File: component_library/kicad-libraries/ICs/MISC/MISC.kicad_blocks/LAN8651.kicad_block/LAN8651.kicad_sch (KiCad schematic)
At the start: 7 parts, among them U1 LAN8651B1-E/LMX

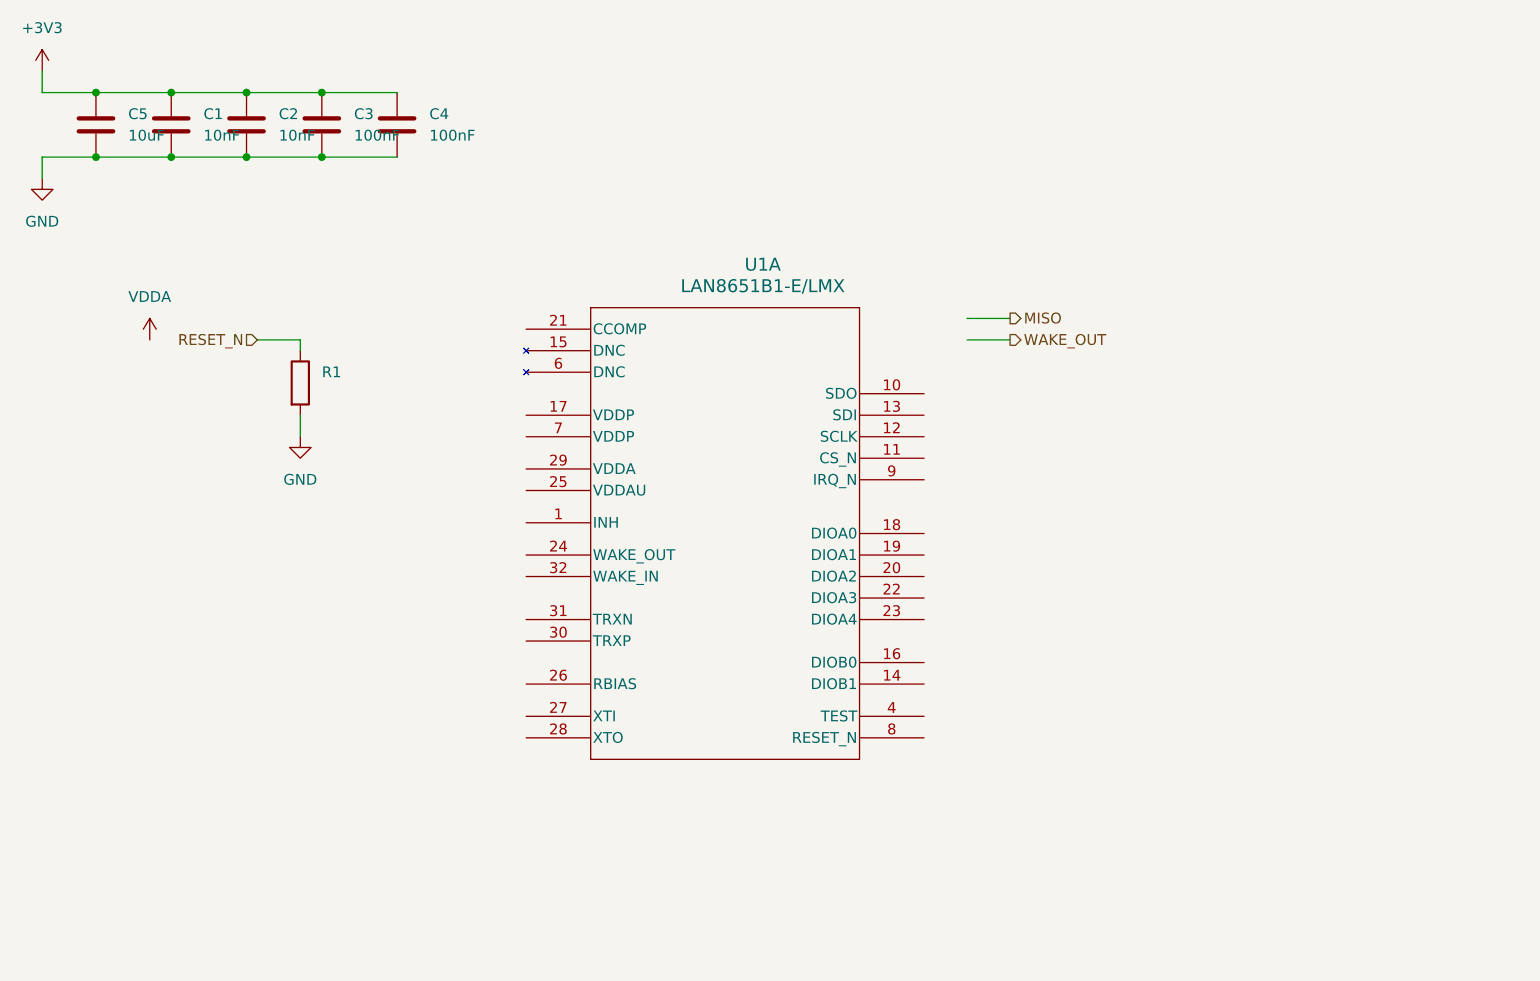
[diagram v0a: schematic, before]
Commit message: added crystal oscillator, finished schematic and layout
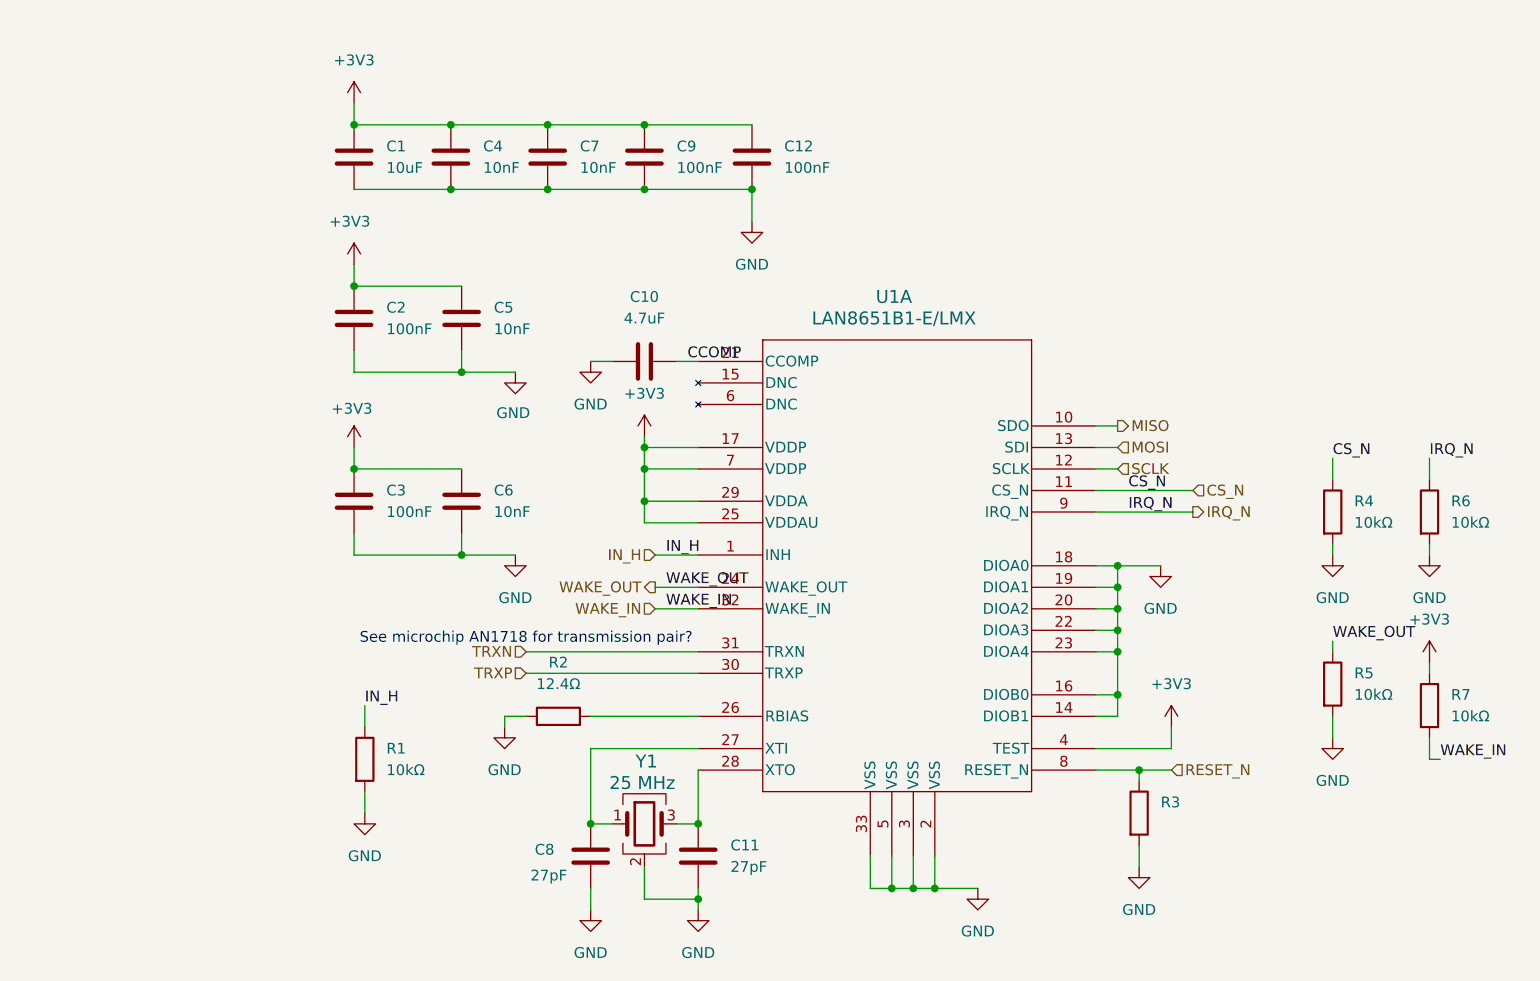
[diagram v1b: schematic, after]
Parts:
- removed C1, C2: 10nF, Capacitor_SMD:C_0402_1005Metric, symbol SSI_Passives:C 10nF 0402 50V X7R 10% Samsung
- removed C4: 100nF, Capacitor_SMD:C_0402_1005Metric, symbol SSI_Passives:C 100nF 0402 50V X7R 10% Samsung
- removed C5: 10uF, Capacitor_SMD:C_1210_3225Metric, symbol SSI_Passives:C 10uF 1210 25V X5R 10% Samsung
- added C1: 10uF, Capacitor_SMD:C_1210_3225Metric, symbol SSI_Passives:C 10uF 1210 25V X5R 10% Samsung
- added C10: 4.7uF, Capacitor_SMD:C_0402_1005Metric, symbol SSI_Passives:C 4.7uF 0402 10V X5R 20% Samsung
- added C11, C8: 27pF, Capacitor_SMD:C_0402_1005Metric, symbol SSI_Passives:C 27pF 0402 50V C0G 5% Samsung
- added C12, C2, C9: 100nF, Capacitor_SMD:C_0402_1005Metric, symbol SSI_Passives:C 100nF 0402 50V X7R 10% Samsung
- added C4, C5, C6, C7: 10nF, Capacitor_SMD:C_0402_1005Metric, symbol SSI_Passives:C 10nF 0402 50V X7R 10% Samsung
- added R2: 12.4Ω, Resistor_SMD:R_0402_1005Metric, symbol SSI_Passives:R 12.4 0402 1% Uniroyal
- added R3, R4, R5, R6, R7: 10kΩ, Resistor_SMD:R_0402_1005Metric, symbol SSI_Passives:R 10k 0402 1% Uniroyal
- added Y1: 25 MHz, SSI_ABM8G:CRYSTAL_ABM8G_ABR, symbol Device:Crystal_GND24
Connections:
- net +3V3: now also U1.17 (VDDP), U1.25 (VDDAU), U1.29 (VDDA), U1.4 (TEST), U1.7 (VDDP), C1.1, C12.1, C2.1, C4.1, C5.1, C6.1, C7.1, C9.1, R7.1
- net GND: now also U1.14 (DIOB1), U1.16 (DIOB0), U1.18 (DIOA0), U1.19 (DIOA1), U1.2 (VSS), U1.20 (DIOA2), U1.22 (DIOA3), U1.23 (DIOA4), U1.3 (VSS), U1.33 (VSS), U1.5 (VSS), C1.2, C10.2, C11.2, C12.2, C2.2, C4.2, C5.2, C6.2, C7.2, C8.2, C9.2, R2.1, R3.2, R4.2, R5.2, R6.2, Y1.2 (G), Y1.4 (G)
- net MISO: now also U1.10 (SDO)
- net RESET_N: now also U1.8 (RESET_N), R3.1; no longer R1.1
- net WAKE_OUT: now also U1.24 (WAKE_OUT), R5.1
- net IN_H: now reaches U1.1 (INH)
- net IN_H: now also R1.1
- net CS_N: now reaches U1.11 (CS_N)
- net CS_N: now also R4.1
- net SCLK: now reaches U1.12 (SCLK)
- net MOSI: now reaches U1.13 (SDI)
- net CCOMP: now reaches U1.21 (CCOMP)
- net CCOMP: now also C10.1
- net at U1.26 (RBIAS): now also R2.2
- net at U1.27 (XTI): now also C8.1, Y1.1
- net at U1.28 (XTO): now also C11.1, Y1.3
- net TRXP: now reaches U1.30 (TRXP)
- net TRXN: now reaches U1.31 (TRXN)
- net WAKE_IN: now reaches U1.32 (WAKE_IN)
- net WAKE_IN: now also R7.2
- net IRQ_N: now reaches U1.9 (IRQ_N)
- net IRQ_N: now also R6.1
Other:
- note added: "See microchip AN1718 for transmission pair?"
